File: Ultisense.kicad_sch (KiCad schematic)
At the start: 39 parts, among them J1 USB_C_Receptacle_USB2.0_14P, J2 Conn_01x02, J3 Micro_SD_Card, SW2 SW_Push, SW3 SW_Push, U1 ESP32-S3-WROOM-1, U2 TPS61023, U3 BQ24075RGT, U4 AP2112K-3.3, U6 USBLC6-2P6, U7 MCP23017_SO

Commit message: finished schematic, starting pcb
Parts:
- removed C1: 22uF, symbol Device:C
- removed C8: 0.1uF, symbol Device:C
- removed D3: LED, symbol Device:LED
- removed R12: 330, symbol Device:R
- added C10, C24, C25, C26: 0.1uF, Capacitor_SMD:C_01005_0402Metric, symbol Device:C
- added C11, C12, C13, C14, C17, C19, C22: 1uF, Capacitor_SMD:C_01005_0402Metric, symbol Device:C
- added C15, C8: 22uF, Capacitor_SMD:CP_Elec_5x5.3, symbol Device:C_Polarized
- added C16, C18: 10uF, Capacitor_SMD:C_0603_1608Metric, symbol Device:C
- added C20, C21: 2.2nF, Capacitor_SMD:C_01005_0402Metric, symbol Device:C
- added C23: 0.47uF, Capacitor_SMD:C_01005_0402Metric, symbol Device:C
- added J5, J8: Conn_01x08, Connector_PinHeader_2.54mm:PinHeader_1x08_P2.54mm_Vertical, symbol Connector_Generic:Conn_01x08
- added J6: Conn_02x02_Odd_Even, Connector_PinHeader_2.54mm:PinHeader_2x02_P2.54mm_Vertical, symbol Connector_Generic:Conn_02x02_Odd_Even
- added J7: Conn_02x08_Top_Bottom, Connector_PinSocket_2.54mm:PinSocket_2x08_P2.54mm_Vertical, symbol Connector_Generic:Conn_02x08_Top_Bottom
- added L2: NFC_ANTENNA, nfc:nfcantenna, symbol Device:L
- added LS1, LS2: Speaker, Connector_PinHeader_2.54mm:PinHeader_2x02_P2.54mm_Vertical, symbol Device:Speaker
- added R16, R4: 4.7K, Resistor_SMD:R_01005_0402Metric, symbol Device:R
- added R17: 470, Resistor_SMD:R_01005_0402Metric, symbol Device:R
- added R18, R19, R20: 10K, Resistor_SMD:R_01005_0402Metric, symbol Device:R
- added TH1: 10K, Resistor_SMD:R_0603_1608Metric, symbol Device:Thermistor_NTC
- added U10: ST25DV04KC-IE6S3, easyeda2kicad:SO-8_L4.9-W3.9-P1.27-LS5.9-BL, symbol easyeda2kicad:ST25DV04KC-IE6S3
- added U12: SSD1306, longscreen:SSD1306, symbol SSD1306:SSD1306
- added U14: ICM-45605, easyeda2kicad:LGA-14_L3.0-W2.5-P0.50-TL, symbol easyeda2kicad:ICM-45605
- added U15: ~, touchpad:Touch_Pad, symbol touch:Touch_Pad
- added U5: MSM261DGT003, easyeda2kicad:MIC-SMD_6P-L4.0-W2.0_LMD4020T261-OC3, symbol MSM261DGT003:MSM261DGT003
- added U8: PAM8403D, Package_SO:SOP-16_3.9x9.9mm_P1.27mm, symbol Amplifier_Audio:PAM8403D
- added U9: PCM5102A, Package_SO:TSSOP-20_4.4x6.5mm_P0.65mm, symbol Audio:PCM5102A
- C2, C3, C6, C9: footprint (none) -> Capacitor_SMD:C_01005_0402Metric
- C4, C5, C7: footprint (none) -> Capacitor_SMD:C_0603_1608Metric
- D1, D2, D4: footprint (none) -> LED_SMD:LED_0603_1608Metric
- J1: footprint (none) -> Connector_USB:USB_C_Receptacle_HRO_TYPE-C-31-M-12
- J2: footprint (none) -> Connector_PinHeader_2.54mm:PinHeader_1x02_P2.54mm_Vertical
- J3: footprint (none) -> easyeda2kicad:TF-SMD_TF-PUSH
- L1: footprint (none) -> easyeda2kicad:IND-SMD_L4.0-W4.0-A
- R1, R10, R11, R13, R14, R15, R2, R3, R5, R6, R8, R9: footprint (none) -> Resistor_SMD:R_01005_0402Metric
- R7: value 10K -> 470; footprint (none) -> Resistor_SMD:R_01005_0402Metric
- SW2, SW3: footprint (none) -> easyeda2kicad:SW-SMD_L3.9-W3.0-P4.45
- U2: footprint (none) -> easyeda2kicad:SOT-563_L1.6-W1.2-P0.50-LS1.6-BR
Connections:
- net +3V3: now also R15.2, C10.1, C11.1, C12.1, C13.1, C15.1, C16.1, C24.1, C25.1, C26.2, J6.1 (Pin_1), J6.3 (Pin_3), R16.1, R18.2, R19.2, R20.2, R4.1, U10.8 (VCC), U12.2 (VDD), U14.12 (AP_CS), U14.5 (VDDIO), U14.8 (VDD), U5.1 (VDD), U9.1 (CPVDD), U9.17 (XSMT), U9.20 (DVDD), U9.8 (AVDD); no longer R15.1
- net +5V: now also C14.1, C22.1, C8.1, U8.12 (~{SHDN}), U8.13 (PVDD), U8.4 (PVDD), U8.5 (~{MUTE}), U8.6 (VDD)
- net GND: now also C10.2, C11.2, C12.2, C13.2, C14.2, C15.2, C16.2, C17.2, C18.2, C20.2, C21.2, C22.2, C23.2, C24.2, C25.2, C26.1, C8.2, J6.2 (Pin_2), J6.4 (Pin_4), TH1.2, U10.4 (VSS), U12.1 (GND), U14.1 (AP_SDO/AP_AD0), U14.6 (GND), U5.2 (GND), U5.5 (GND), U5.6 (L/R), U8.11 (GND), U8.15 (PGND), U8.2 (PGND), U9.16 (FMT), U9.19 (DGND), U9.3 (CPGND), U9.9 (AGND); no longer R7.2
- net IO1: now also U7.20 (INTA)
- net IO14: now also U9.15 (LRCK)
- net IO15: now also U9.14 (DIN)
- net IO16: now also U9.13 (BCK)
- net IO4: now also U5.4 (CLK)
- net IO5: now also U5.3 (DATA)
- net IO6: now also U15.1 (Touch_Pad)
- net IO7: now also J5.6 (Pin_6)
- net MISO: now also J5.3 (Pin_3), R20.1
- net MOSI: now also J5.5 (Pin_5), R18.1
- net SCK: now also J5.4 (Pin_4), R19.1
- net SCL: now also J5.7 (Pin_7), R16.2, U10.6 (SCL), U12.3 (SCK), U14.13 (AP_SCL/AP_SCLK)
- net SDA: now also J5.8 (Pin_8), R4.2, U10.5 (SDA), U12.4 (SDA), U14.14 (AP_SDA/AP_SDIO/AP_SDI)
- net at U3.1 (TS): now also TH1.1; no longer R7.1
- net GPB0: now reaches U7.1 (GPB0)
- net GPB0: now also J7.9 (Pin_9)
- net GPB1: now reaches U7.2 (GPB1)
- net GPB1: now also J7.10 (Pin_10)
- net GPA0: now reaches U7.21 (GPA0)
- net GPA0: now also J7.1 (Pin_1)
- net GPA1: now reaches U7.22 (GPA1)
- net GPA1: now also J7.2 (Pin_2)
- net GPA2: now reaches U7.23 (GPA2)
- net GPA2: now also J7.3 (Pin_3)
- net GPA3: now reaches U7.24 (GPA3)
- net GPA3: now also J7.4 (Pin_4)
- net GPA4: now reaches U7.25 (GPA4)
- net GPA4: now also J7.5 (Pin_5)
- net GPA5: now reaches U7.26 (GPA5)
- net GPA5: now also J7.6 (Pin_6)
- net GPA6: now reaches U7.27 (GPA6)
- net GPA6: now also J7.7 (Pin_7)
- net GPA7: now reaches U7.28 (GPA7)
- net GPA7: now also J7.8 (Pin_8)
- net GPB2: now reaches U7.3 (GPB2)
- net GPB2: now also J7.11 (Pin_11)
- net GPB3: now reaches U7.4 (GPB3)
- net GPB3: now also J7.12 (Pin_12)
- net GPB4: now reaches U7.5 (GPB4)
- net GPB4: now also J7.13 (Pin_13)
- net GPB5: now reaches U7.6 (GPB5)
- net GPB5: now also J7.14 (Pin_14)
- net GPB6: now reaches U7.7 (GPB6)
- net GPB6: now also J7.15 (Pin_15)
- net GPB7: now reaches U7.8 (GPB7)
- net GPB7: now also J7.16 (Pin_16)
- net IO17: now reaches U1.10 (IO17)
- net IO17: now also U14.4 (INT1/INT)
- net IO18: now reaches U1.11 (IO18)
- net IO18: now also J5.2 (Pin_2)
- net IO21: now reaches U1.23 (IO21)
- net IO21: now also J5.1 (Pin_1)
- net IO47: now reaches U1.24 (IO47)
- net IO47: now also J8.8 (Pin_8)
- net IO48: now reaches U1.25 (IO48)
- net IO48: now also U10.7 (GPO)
- net IO38: now reaches U1.31 (IO38)
- net IO38: now also J8.3 (Pin_3)
- net IO39: now reaches U1.32 (IO39)
- net IO39: now also J8.4 (Pin_4)
- net IO40: now reaches U1.33 (IO40)
- net IO40: now also J8.5 (Pin_5)
- net IO41: now reaches U1.34 (IO41)
- net IO41: now also J8.6 (Pin_6)
- net IO42: now reaches U1.35 (IO42)
- net IO42: now also J8.7 (Pin_7)
- net RXD0: now reaches U1.36 (RXD0)
- net RXD0: now also J8.2 (Pin_2)
- net TXD0: now reaches U1.37 (TXD0)
- net TXD0: now also J8.1 (Pin_1)
- net CS renamed IO10
- net IO10: now also R15.1; no longer R15.2
- net IO0 renamed RESET
- net IO3: no longer names the net of U1.15 (IO3)
- net IO3: no longer U7.20 (INTA)
- new net: LS2.1, U8.1 (LOUT+)
- new net: C21.1, R17.1, U8.10 (INR)
- new net: LS1.2, U8.14 (ROUT-)
- new net: LS1.1, U8.16 (ROUT+)
- new net: LS2.2, U8.3 (LOUT-)
- new net: C20.1, R7.2, U8.7 (INL)
- new net: C23.1, U8.8 (VREF)
- new net: R17.2, U9.7 (OUTR)
- new net: C17.1, U9.5 (VNEG)
- new net: C18.1, U9.18 (LDOO)
- new net: L2.1, U10.3 (AC1)
- new net: L2.2, U10.2 (AC0)
- new net: U9.10 (DEMP), U9.11 (FLT), U9.12 (SCK)
- new net: C19.1, U9.2 (CAPP)
- new net: C19.2, U9.4 (CAPM)
- new net: R7.1, U9.6 (OUTL)
- no-connect marks 4 -> 17
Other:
- note added: "audio path"
- moved on the sheet: C2, C4, C5, C6, C7, C9, D4, J3, L1, R10, R11, R13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

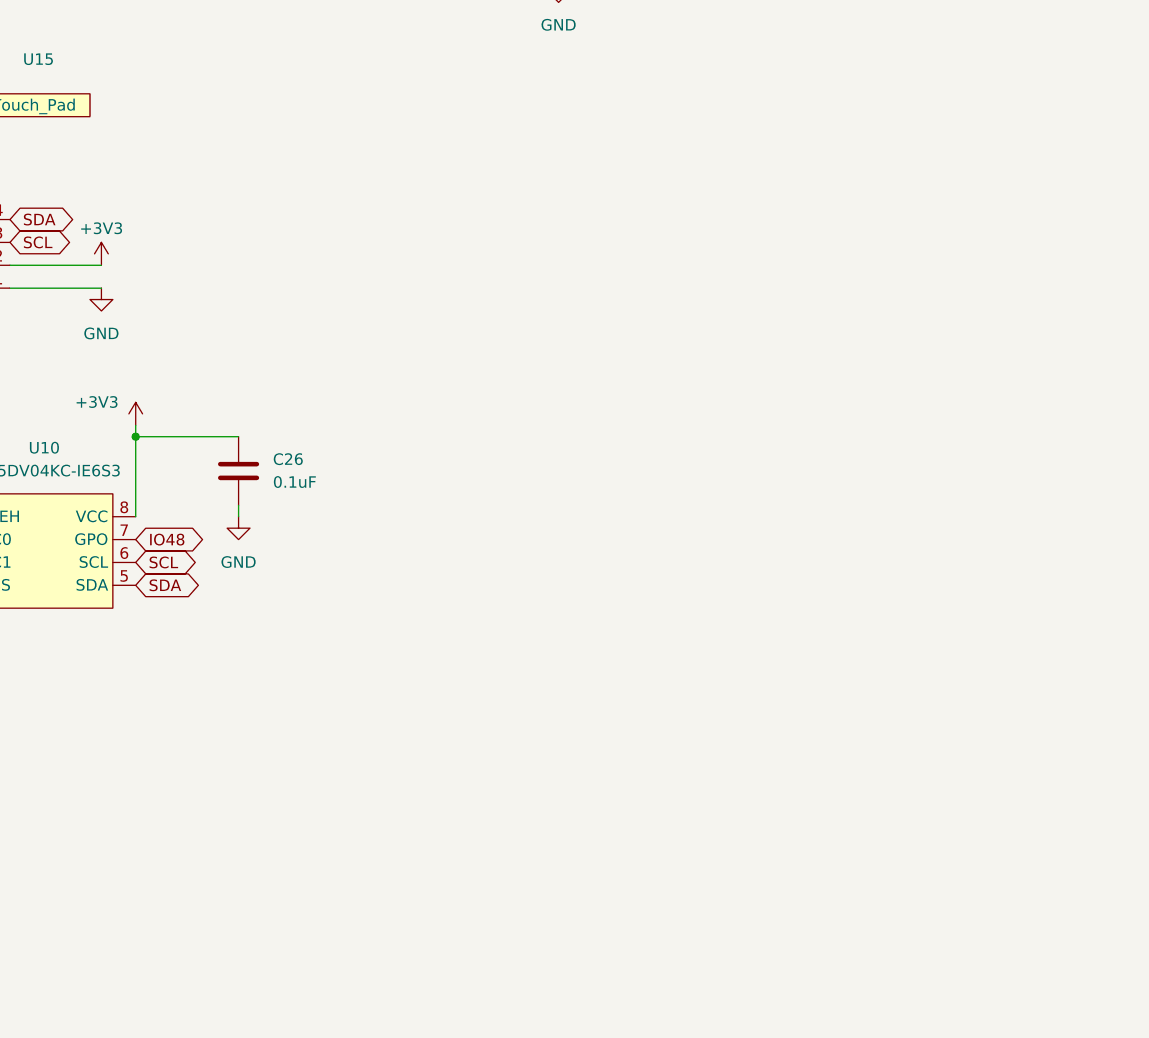
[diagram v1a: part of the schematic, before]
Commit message: actually fr done schematic, figured out nfc antenna
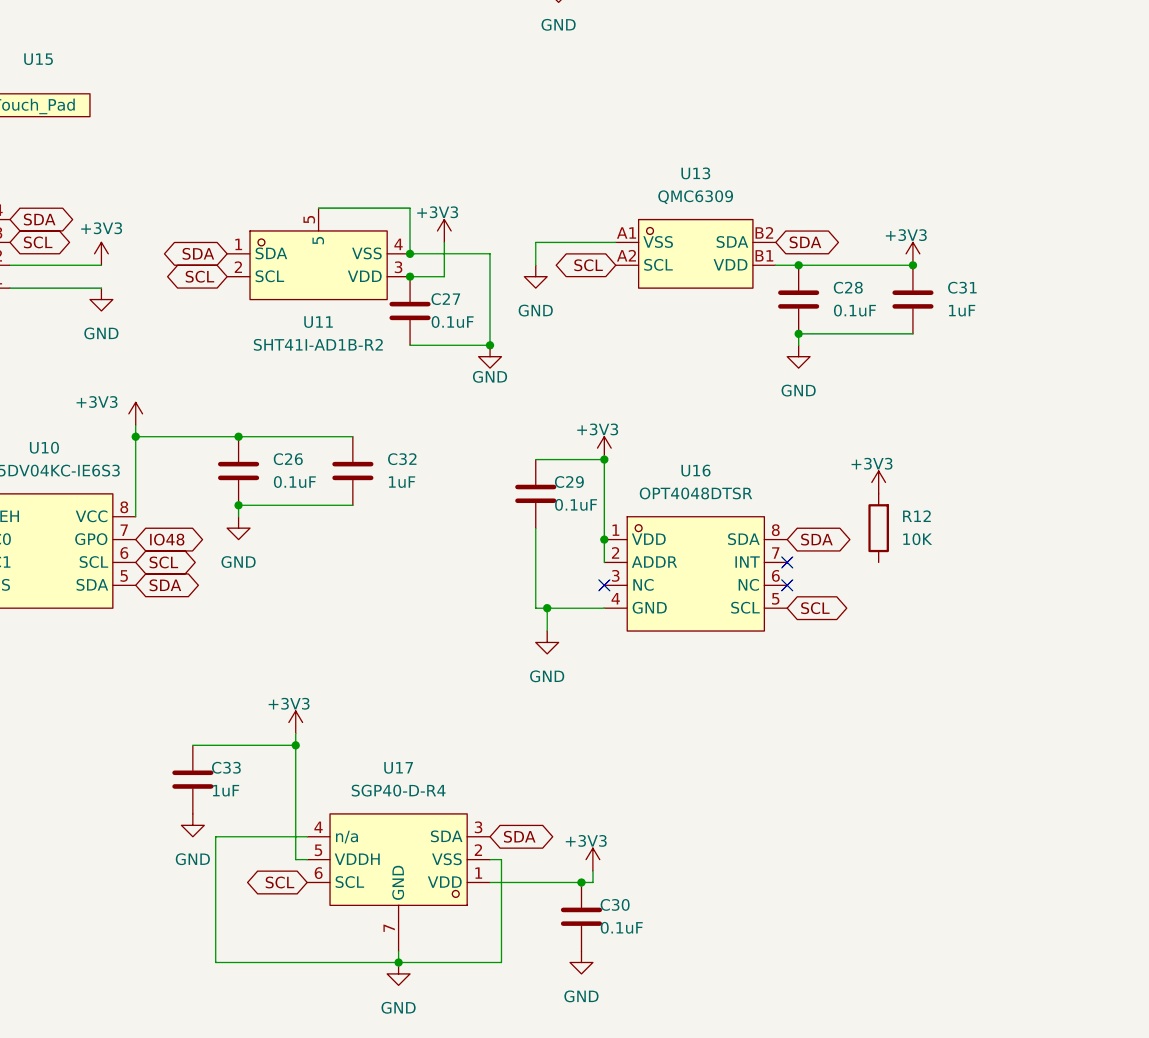
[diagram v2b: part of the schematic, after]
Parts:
- added C27, C28, C29, C30: 0.1uF, Capacitor_SMD:C_01005_0402Metric, symbol Device:C
- added C31, C32, C33: 1uF, Capacitor_SMD:C_01005_0402Metric, symbol Device:C
- added R12: 10K, Resistor_SMD:R_01005_0402Metric, symbol Device:R
- added U11: SHT41I-AD1B-R2, easyeda2kicad:SENSOR-SMD_4P-L1.5-W1.5-P1.00-TL, symbol easyeda2kicad:SHT41I-AD1B-R2
- added U13: QMC6309, easyeda2kicad:X1-WLB0808-4_L0.8-W0.8-P0.40-TL, symbol easyeda2kicad:QMC6309
- added U16: OPT4048DTSR, easyeda2kicad:SOT-5X3-8_L2.1-W1.2-P0.50-LS1.9-BL, symbol easyeda2kicad:OPT4048DTSR
- added U17: SGP40-D-R4, easyeda2kicad:DFN-6_L2.4-W2.4-P0.80-TL-EP, symbol easyeda2kicad:SGP40-D-R4
- L2: footprint nfc:nfcantenna -> PCB Coils:NFC_Coil
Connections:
- net +3V3: now also C27.2, C28.2, C29.2, C30.2, C31.2, C32.2, C33.2, R12.2, U11.3 (VDD), U13.B1 (VDD), U16.1 (VDD), U16.2 (ADDR), U17.1 (VDD), U17.5 (VDDH)
- net GND: now also C27.1, C28.1, C29.1, C30.1, C31.1, C32.1, C33.1, U11.4 (VSS), U11.5, U13.A1 (VSS), U16.4 (GND), U17.2 (VSS), U17.4 (n/a), U17.7 (GND)
- net SCL: now also U11.2 (SCL), U13.A2 (SCL), U16.5 (SCL), U17.6 (SCL)
- net SDA: now also U11.1 (SDA), U13.B2 (SDA), U16.8 (SDA), U17.3 (SDA)
- no-connect marks 17 -> 20

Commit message: layout done
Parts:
- removed C22: 1uF, Capacitor_SMD:C_01005_0402Metric, symbol Device:C
- removed R12: 10K, Resistor_SMD:R_01005_0402Metric, symbol Device:R
- added C34, C36: 0.1uF, Capacitor_SMD:C_01005_0402Metric, symbol Device:C
- LS1, LS2: footprint Connector_PinHeader_2.54mm:PinHeader_2x02_P2.54mm_Vertical -> Connector_PinHeader_2.54mm:PinHeader_2x01_P2.54mm_Vertical
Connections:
- net +3V3: now also C36.1
- net GND: now also C34.2, C36.2
- net VBUS: now also C34.1
- net D+: now reaches J1.A6 (D+), J1.B6 (D+), U6.3 (I/O2)
- net D-: now reaches J1.A7 (D-), J1.B7 (D-), U6.1 (I/O1)
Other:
- note added: "headers and multiplexer"
- note added: "mcu and output"
- note added: "sd card"
- note added: "sensors"
- moved on the sheet: C15, C2, C24, C25, C26, C27, C28, C29, C30, C31, C32, C33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

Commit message: routing almost done; backup:
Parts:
- removed J5, J8: Conn_01x08, Connector_PinHeader_2.54mm:PinHeader_1x08_P2.54mm_Vertical, symbol Connector_Generic:Conn_01x08
- added J5: Conn_02x08_Odd_Even, Connector_PinHeader_2.54mm:PinHeader_2x08_P2.54mm_Vertical, symbol Connector_Generic:Conn_02x08_Odd_Even
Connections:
- net GND: now also U9.10 (DEMP), U9.11 (FLT), U9.12 (SCK)
- net IO18: now also J5.13 (Pin_13)
- net IO21: now also J5.9 (Pin_9)
- net IO38: now also J5.8 (Pin_8)
- net IO39: now also J5.5 (Pin_5)
- net IO40: now also J5.6 (Pin_6)
- net IO41: now also J5.3 (Pin_3)
- net IO42: now also J5.4 (Pin_4)
- net IO47: now also J5.10 (Pin_10)
- net IO7: now also J5.7 (Pin_7)
- net MISO: now also J5.12 (Pin_12)
- net MOSI: now also J5.14 (Pin_14)
- net RXD0: now also J5.2 (Pin_2)
- net SCK: now also J5.11 (Pin_11)
- net SCL: now also J5.16 (Pin_16)
- net SDA: now also J5.15 (Pin_15)
- net TXD0: now also J5.1 (Pin_1)

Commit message: done
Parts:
- C4, C5, C7: value 4.7uF -> 10uF
- L2, U15: now left out of the parts list
- R13: value 330 -> 470
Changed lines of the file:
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@@
 			)
 		)
-		(property "Value" "4.7uF"
+		(property "Value" "10uF"
 			(at 125.73 42.164 0)
 			(effects
@@
 		(unit 1)
 		(exclude_from_sim no)
-		(in_bom yes)
+		(in_bom no)
 		(on_board yes)
 		(dnp no)
@@
 		(unit 1)
 		(exclude_from_sim no)
-		(in_bom yes)
+		(in_bom no)
 		(on_board yes)
 		(dnp no)
@@
 			)
 		)
-		(property "Value" "4.7uF"
+		(property "Value" "10uF"
 			(at 142.24 41.91 0)
 			(effects
@@
 			)
 		)
-		(property "Value" "4.7uF"
+		(property "Value" "10uF"
 			(at 176.53 31.75 0)
 			(effects
@@
 			)
 		)
-		(property "Value" "330"
-			(at 287.782 152.908 0)
+		(property "Value" "470"
+			(at 287.528 152.908 0)
 			(effects
 				(font

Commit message: fixed nfc
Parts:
- removed U15: ~, touchpad:Touch_Pad, symbol touch:Touch_Pad
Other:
- moved on the sheet: C15, C2, C26, C27, C30, C32, C33, C9, D4, J3, J5, J6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

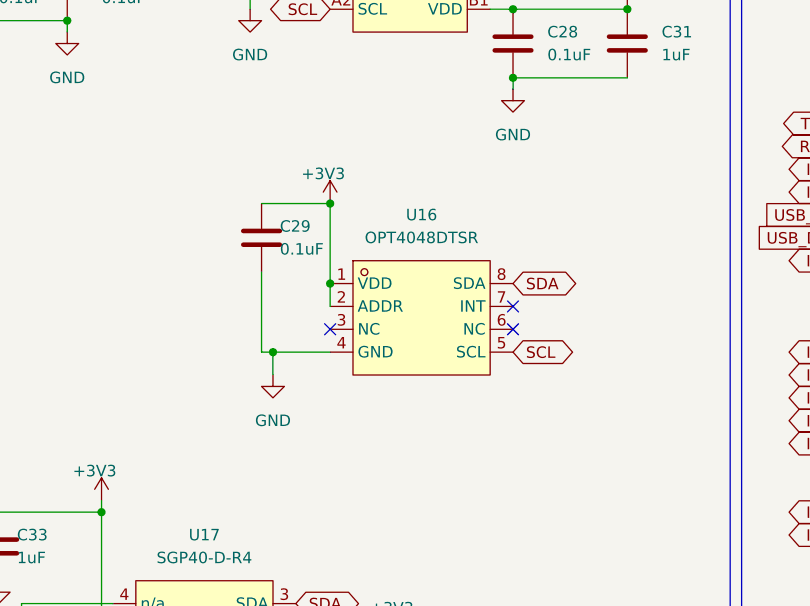
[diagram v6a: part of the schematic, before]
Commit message: replaced out of stock light sensor
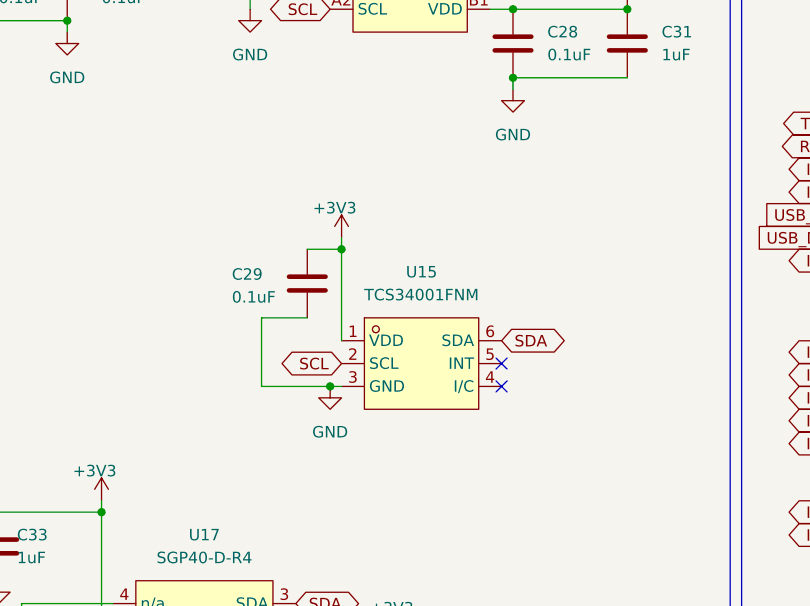
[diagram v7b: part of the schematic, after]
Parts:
- removed U16: OPT4048DTSR, easyeda2kicad:SOT-5X3-8_L2.1-W1.2-P0.50-LS1.9-BL, symbol easyeda2kicad:OPT4048DTSR
- added U15: TCS34001FNM, easyeda2kicad:DFN-6_L2.4-W2.0-P0.65-BL, symbol easyeda2kicad:TCS34001FNM
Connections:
- net +3V3: now also U15.1 (VDD)
- net GND: now also U15.3 (GND)
- net SCL: now also U15.2 (SCL)
- net SDA: now also U15.6 (SDA)
- no-connect marks 20 -> 19
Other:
- moved on the sheet: C29

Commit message: replaced 01005 with 0201, fixed a few other things, reordering
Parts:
- C10, C2, C24, C25, C26, C27, C28, C29, C30, C34, C36, C9: value 0.1uF -> 1uF; footprint Capacitor_SMD:C_01005_0402Metric -> Capacitor_SMD:C_0201_0603Metric
- C11, C12, C13, C14, C17, C19, C3, C31, C32, C33, C6: value 1uF -> 4.7uF; footprint Capacitor_SMD:C_01005_0402Metric -> Capacitor_SMD:C_0201_0603Metric
- C15, C8: footprint Capacitor_SMD:CP_Elec_5x5.3 -> Capacitor_SMD:CP_Elec_4x5.4
- C20, C21, C23: footprint Capacitor_SMD:C_01005_0402Metric -> Capacitor_SMD:C_0402_1005Metric
- R1, R10, R11, R13, R14, R15, R16, R17, R18, R19, R2, R20, R3, R4, R5, R6, R7, R8, R9: footprint Resistor_SMD:R_01005_0402Metric -> Resistor_SMD:R_0201_0603Metric
